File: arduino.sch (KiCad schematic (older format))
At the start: 16 parts

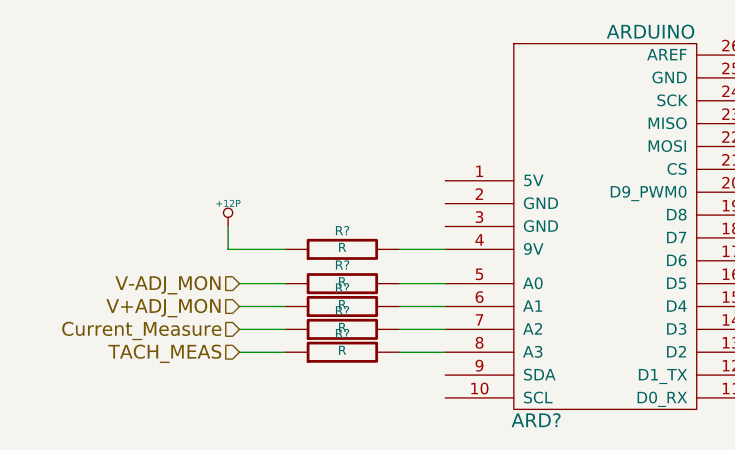
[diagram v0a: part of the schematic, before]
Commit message: Module 3 Unit 15
Choosing Components For The Power Control, Conditioning, Monitoring
Module
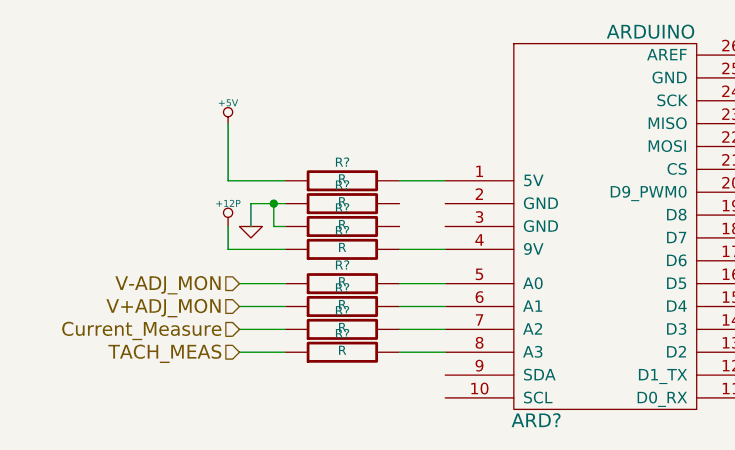
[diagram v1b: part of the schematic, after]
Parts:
- added R? (x3): R, ~, symbol R
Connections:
- net GND: now also R?.1, R?.1
- net at ARD?.1 (5V): now also R?.2
- new net +5V: R?.1
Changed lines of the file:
@@
 Sheet 2 9
 Title ""
-Date "16 feb 2014"
+Date "22 feb 2014"
 Rev ""
 Comp ""
@@
 Wire Wire Line
 	3250 3950 3250 3850
+$Comp
+L R R?
+U 1 1 5308D2F7
+P 3750 3650
+F 0 "R?" V 3830 3650 40  0000 C CNN
+F 1 "R" V 3757 3651 40  0000 C CNN
+F 2 "~" V 3680 3650 30  0000 C CNN
+F 3 "~" H 3750 3650 30  0000 C CNN
+	1    3750 3650
+	0    -1   -1   0
+$EndComp
+Wire Wire Line
+	4000 3650 4200 3650
+Wire Wire Line
+	3500 3650 3250 3650
+Wire Wire Line
+	3250 3650 3250 3400
+$Comp
+L +5V #PWR?
+U 1 1 5308D351
+P 3250 3400
+F 0 "#PWR?" H 3250 3490 20  0001 C CNN
+F 1 "+5V" H 3250 3490 30  0000 C CNN
+F 2 "" H 3250 3400 60  0000 C CNN
+F 3 "" H 3250 3400 60  0000 C CNN
+	1    3250 3400
+	1    0    0    -1
+$EndComp
+$Comp
+L R R?
+U 1 1 5308D35E
+P 3750 3750
+F 0 "R?" V 3830 3750 40  0000 C CNN
+F 1 "R" V 3757 3751 40  0000 C CNN
+F 2 "~" V 3680 3750 30  0000 C CNN
+F 3 "~" H 3750 3750 30  0000 C CNN
+	1    3750 3750
+	0    -1   -1   0
+$EndComp
+$Comp
+L R R?
+U 1 1 5308D364
+P 3750 3850
+F 0 "R?" V 3830 3850 40  0000 C CNN
+F 1 "R" V 3757 3851 40  0000 C CNN
+F 2 "~" V 3680 3850 30  0000 C CNN
+F 3 "~" H 3750 3850 30  0000 C CNN
+	1    3750 3850
+	0    -1   -1   0
+$EndComp
+$Comp
+L GND #PWR?
+U 1 1 5308D36C
+P 3350 3850
+F 0 "#PWR?" H 3350 3850 30  0001 C CNN
+F 1 "GND" H 3350 3780 30  0001 C CNN
+F 2 "" H 3350 3850 60  0000 C CNN
+F 3 "" H 3350 3850 60  0000 C CNN
+	1    3350 3850
+	1    0    0    -1
+$EndComp
+Wire Wire Line
+	3500 3850 3450 3850
+Wire Wire Line
+	3450 3850 3450 3750
+Wire Wire Line
+	3350 3750 3500 3750
+Wire Wire Line
+	3350 3750 3350 3850
+Connection ~ 3450 3750
 $EndSCHEMATC
